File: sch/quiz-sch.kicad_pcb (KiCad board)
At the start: 2 copper layers, 45 x 100 mm, 72 parts, among them IC1 74HC4050, J1 USB_B_Micro, J2 AVR ISP, Q1 BC817, Q2 BC817, SW1 MUTE_SW, SW2 PROG_SW, SW3 SW_UP, SW4 SW_DOWN, SW5 SW_LEFT, SW6 SW_RIGHT, SW7 SW_ENTER, SW8 SW_MENU, U1 MCP73831-2-OT, U2 ATmega328P-AU, U3 TPS61092, U4 LD1117S33TR_SOT223, U5 74HCT4051, U6 FT232RL, U7 NOKIA5510, U8 24LC16BT-I_OT, Y1 16MHz

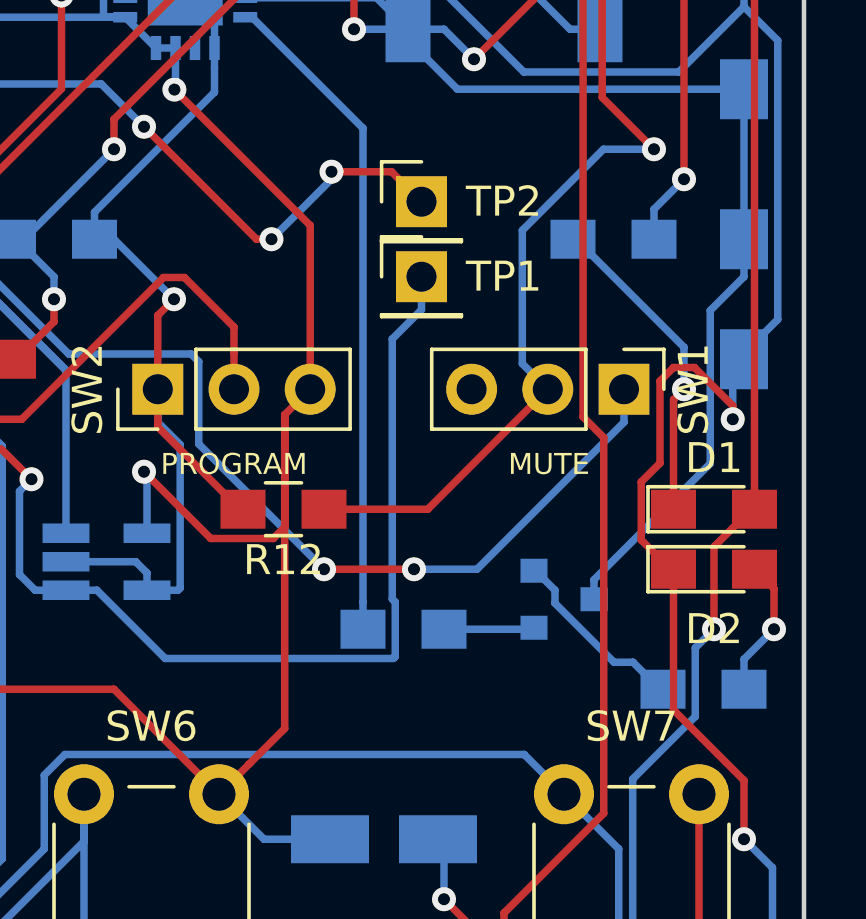
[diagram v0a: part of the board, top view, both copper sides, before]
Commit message: Added PDF of schematic
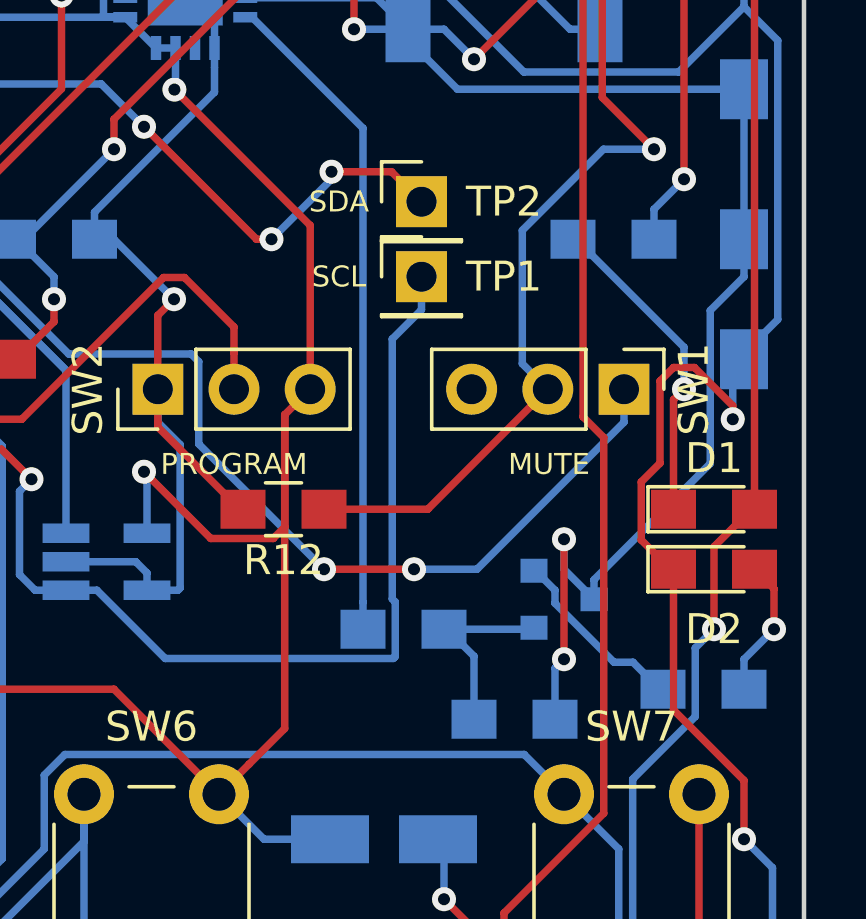
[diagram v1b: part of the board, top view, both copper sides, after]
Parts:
- added R25: 100K, Resistors_SMD:R_0805_HandSoldering, B.Cu at (85.3, 123.0)
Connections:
- net 5V renamed +5V
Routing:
- net +BATT: track 92.5 -> 101.0 mm, vias 4 -> 6
- net Net-(Q1-Pad1): track 3.02 -> 6.49 mm
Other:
- board text added: "SCL"
- board text added: "SDA"
